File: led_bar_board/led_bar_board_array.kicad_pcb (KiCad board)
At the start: 2 copper layers, 90 x 98 mm, 720 parts, among them P1 Conn_01x01_Pin, P2 Conn_01x01_Pin, P3 Conn_01x01_Pin

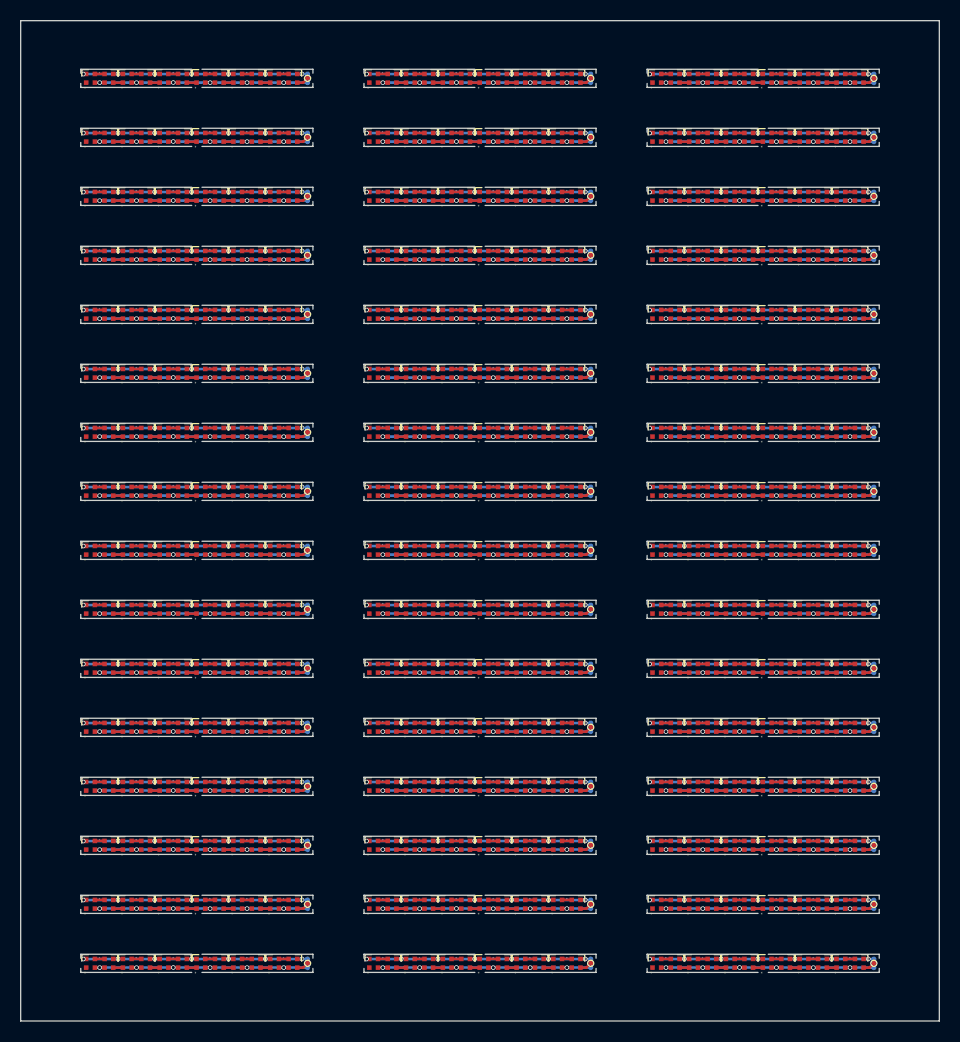
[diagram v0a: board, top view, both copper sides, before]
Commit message: feat(led_bar): modify shape and pad
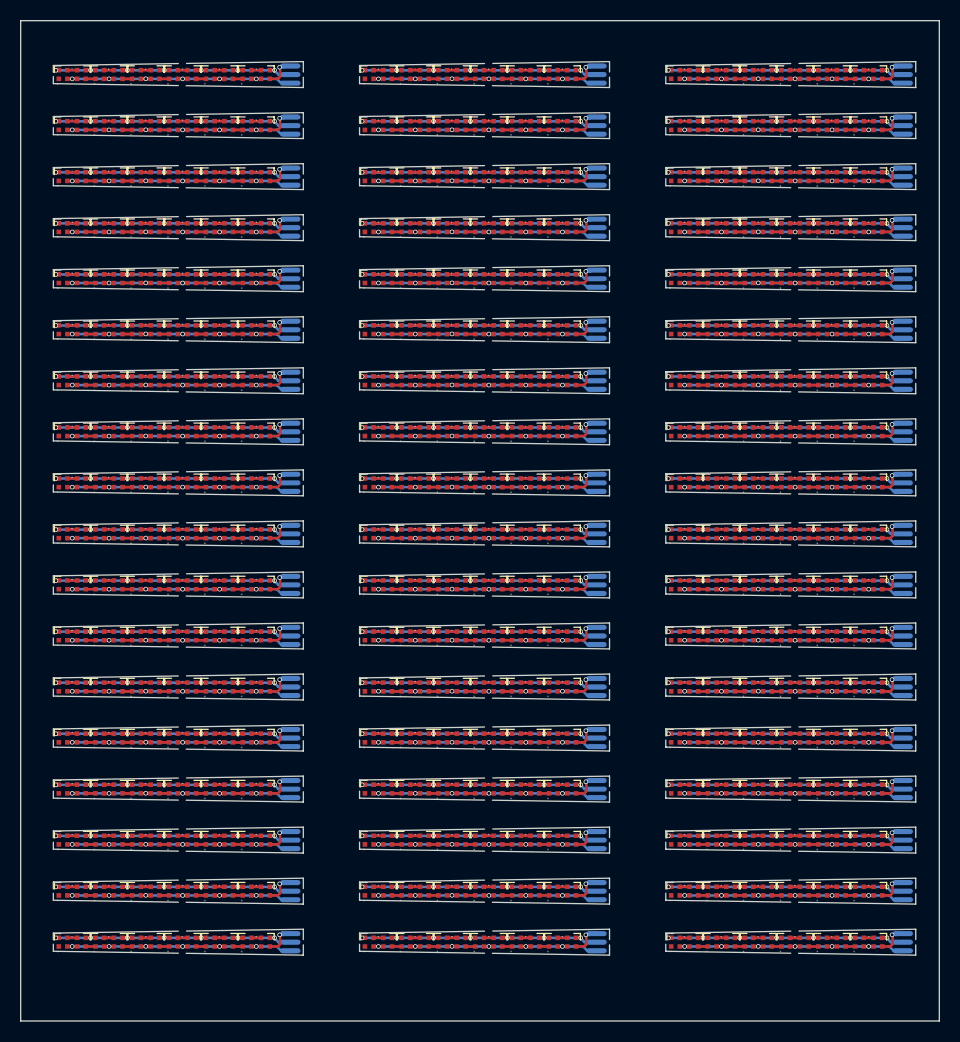
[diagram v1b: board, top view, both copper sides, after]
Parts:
- removed the D1 at (176.3, 62.4)
- removed the D1 at (120.8, 102.9)
- removed the D1 at (148.5, 62.4)
- removed the D1 at (120.8, 126.0)
- removed the D1 at (120.8, 50.9)
- removed the D1 at (120.8, 85.6)
- removed the D1 at (176.3, 137.6)
- removed the D1 at (148.5, 126.0)
- removed the D1 at (148.5, 108.7)
- removed the D1 at (176.3, 50.9)
- removed the D1 at (120.8, 108.7)
- removed the D1 at (148.5, 102.9)
- removed the D1 at (120.8, 68.2)
- removed the D1 at (176.3, 120.2)
- removed the D1 at (176.3, 79.8)
- removed the D1 at (148.5, 114.5)
- removed the D1 at (176.3, 114.5)
- removed the D1 at (120.8, 97.1)
- removed the D1 at (120.8, 74.0)
- removed the D1 at (148.5, 91.3)
- removed the D1 at (148.5, 56.7)
- removed the D1 at (148.5, 131.8)
- removed the D1 at (176.3, 102.9)
- removed the D1 at (148.5, 50.9)
- removed the D1 at (176.3, 97.1)
- removed the D1 at (148.5, 97.1)
- removed the D1 at (120.8, 62.4)
- removed the D1 at (148.5, 120.2)
- removed the D1 at (148.5, 74.0)
- removed the D1 at (120.8, 56.7)
- removed the D1 at (120.8, 131.8)
- removed the D1 at (120.8, 120.2)
- removed the D1 at (120.8, 114.5)
- removed the D1 at (176.3, 126.0)
- removed the D1 at (148.5, 68.2)
- removed the D1 at (176.3, 74.0)
- removed the D1 at (148.5, 85.6)
- removed the D1 at (176.3, 91.3)
- removed the D1 at (176.3, 85.6)
- removed the D1 at (148.5, 137.6)
- removed the D1 at (176.3, 68.2)
- removed the D1 at (176.3, 56.7)
- removed the D1 at (120.8, 137.6)
- removed the D1 at (176.3, 108.7)
- removed the D1 at (120.8, 79.8)
- removed the D1 at (176.3, 131.8)
- removed the D1 at (148.5, 79.8)
- removed the D1 at (120.8, 91.3)
- removed the D10 at (104.6, 108.7)
- removed the D10 at (132.3, 97.1)
- removed the D10 at (104.6, 79.8)
- removed the D10 at (160.0, 85.6)
- removed the D10 at (160.0, 97.1)
- removed the D10 at (104.6, 85.6)
- removed the D10 at (104.6, 56.7)
- removed the D10 at (160.0, 50.9)
- removed the D10 at (160.0, 126.0)
- removed the D10 at (132.3, 137.6)
- removed the D10 at (104.6, 114.5)
- removed the D10 at (160.0, 114.5)
- removed the D10 at (160.0, 74.0)
- removed the D10 at (132.3, 102.9)
- removed the D10 at (104.6, 91.3)
- removed the D10 at (132.3, 85.6)
- removed the D10 at (132.3, 108.7)
- removed the D10 at (132.3, 68.2)
- removed the D10 at (160.0, 102.9)
- removed the D10 at (104.6, 102.9)
- removed the D10 at (104.6, 137.6)
- removed the D10 at (132.3, 91.3)
- removed the D10 at (160.0, 131.8)
- removed the D10 at (160.0, 68.2)
- removed the D10 at (104.6, 97.1)
- removed the D10 at (104.6, 50.9)
- removed the D10 at (160.0, 62.4)
- removed the D10 at (104.6, 120.2)
- removed the D10 at (160.0, 56.7)
- removed the D10 at (132.3, 131.8)
- removed the D10 at (160.0, 91.3)
- removed the D10 at (132.3, 79.8)
- removed the D10 at (132.3, 56.7)
- removed the D10 at (104.6, 126.0)
- removed the D10 at (160.0, 108.7)
- removed the D10 at (132.3, 62.4)
- removed the D10 at (104.6, 74.0)
- removed the D10 at (104.6, 68.2)
- removed the D10 at (132.3, 120.2)
- removed the D10 at (132.3, 74.0)
- removed the D10 at (132.3, 114.5)
- removed the D10 at (104.6, 62.4)
- removed the D10 at (132.3, 50.9)
- removed the D10 at (160.0, 79.8)
- removed the D10 at (160.0, 137.6)
- removed the D10 at (160.0, 120.2)
- removed the D10 at (132.3, 126.0)
- removed the D10 at (104.6, 131.8)
- removed the D11 at (158.2, 108.7)
- removed the D11 at (102.8, 74.0)
- removed the D11 at (102.8, 114.5)
- removed the D11 at (102.8, 56.7)
- removed the D11 at (130.5, 120.2)
- removed the D11 at (130.5, 126.0)
- removed the D11 at (158.2, 91.3)
- removed the D11 at (158.2, 74.0)
- removed the D11 at (158.2, 50.9)
- removed the D11 at (158.2, 126.0)
- removed the D11 at (158.2, 79.8)
- removed the D11 at (130.5, 50.9)
- removed the D11 at (130.5, 68.2)
- removed the D11 at (102.8, 108.7)
- removed the D11 at (102.8, 126.0)
- removed the D11 at (158.2, 68.2)
- removed the D11 at (130.5, 91.3)
- removed the D11 at (102.8, 79.8)
- removed the D11 at (158.2, 131.8)
- removed the D11 at (102.8, 85.6)
- removed the D11 at (102.8, 50.9)
- removed the D11 at (130.5, 56.7)
- removed the D11 at (158.2, 85.6)
- removed the D11 at (102.8, 102.9)
- removed the D11 at (130.5, 137.6)
- removed the D11 at (158.2, 114.5)
- removed the D11 at (130.5, 85.6)
- removed the D11 at (102.8, 97.1)
- removed the D11 at (158.2, 56.7)
- removed the D11 at (130.5, 114.5)
- removed the D11 at (158.2, 62.4)
- removed the D11 at (130.5, 131.8)
- removed the D11 at (130.5, 108.7)
- removed the D11 at (158.2, 97.1)
- removed the D11 at (158.2, 137.6)
- removed the D11 at (130.5, 74.0)
- removed the D11 at (130.5, 102.9)
- removed the D11 at (102.8, 91.3)
- removed the D11 at (158.2, 120.2)
- removed the D11 at (102.8, 62.4)
- removed the D11 at (130.5, 79.8)
- removed the D11 at (102.8, 131.8)
- removed the D11 at (102.8, 137.6)
- removed the D11 at (130.5, 97.1)
- removed the D11 at (102.8, 68.2)
- removed the D11 at (102.8, 120.2)
- removed the D11 at (158.2, 102.9)
- removed the D11 at (130.5, 62.4)
- removed the D12 at (128.7, 79.8)
- removed the D12 at (101.0, 85.6)
- removed the D12 at (128.7, 120.2)
- removed the D12 at (156.4, 126.0)
- removed the D12 at (156.4, 85.6)
- removed the D12 at (156.4, 74.0)
- removed the D12 at (101.0, 62.4)
- removed the D12 at (128.7, 50.9)
- removed the D12 at (128.7, 68.2)
- removed the D12 at (101.0, 131.8)
- removed the D12 at (156.4, 91.3)
- removed the D12 at (128.7, 102.9)
- removed the D12 at (128.7, 126.0)
- removed the D12 at (156.4, 79.8)
- removed the D12 at (101.0, 102.9)
- removed the D12 at (128.7, 131.8)
- removed the D12 at (128.7, 108.7)
- removed the D12 at (156.4, 62.4)
- removed the D12 at (128.7, 85.6)
- removed the D12 at (101.0, 108.7)
- removed the D12 at (128.7, 74.0)
- removed the D12 at (156.4, 120.2)
- removed the D12 at (128.7, 91.3)
- removed the D12 at (101.0, 137.6)
- removed the D12 at (128.7, 114.5)
- removed the D12 at (101.0, 79.8)
- removed the D12 at (156.4, 102.9)
- removed the D12 at (101.0, 74.0)
- removed the D12 at (156.4, 131.8)
- removed the D12 at (156.4, 68.2)
- removed the D12 at (128.7, 56.7)
- removed the D12 at (101.0, 50.9)
- removed the D12 at (128.7, 62.4)
- removed the D12 at (101.0, 120.2)
- removed the D12 at (101.0, 68.2)
- removed the D12 at (101.0, 114.5)
- removed the D12 at (156.4, 137.6)
- removed the D12 at (156.4, 50.9)
- removed the D12 at (128.7, 97.1)
- removed the D12 at (101.0, 91.3)
- removed the D12 at (128.7, 137.6)
- removed the D12 at (101.0, 56.7)
- removed the D12 at (156.4, 56.7)
- removed the D12 at (101.0, 97.1)
- removed the D12 at (156.4, 108.7)
- removed the D12 at (156.4, 114.5)
- removed the D12 at (101.0, 126.0)
- removed the D12 at (156.4, 97.1)
- removed the D2 at (119.0, 68.2)
- removed the D2 at (146.7, 50.9)
- removed the D2 at (119.0, 74.0)
- removed the D2 at (119.0, 126.0)
- removed the D2 at (119.0, 50.9)
- removed the D2 at (146.7, 79.8)
- removed the D2 at (146.7, 120.2)
- removed the D2 at (119.0, 62.4)
- removed the D2 at (146.7, 62.4)
- removed the D2 at (146.7, 68.2)
- removed the D2 at (146.7, 74.0)
- removed the D2 at (119.0, 85.6)
- removed the D2 at (119.0, 131.8)
- removed the D2 at (174.5, 91.3)
- removed the D2 at (146.7, 126.0)
- removed the D2 at (146.7, 97.1)
- removed the D2 at (119.0, 91.3)
- removed the D2 at (119.0, 137.6)
- removed the D2 at (174.5, 74.0)
- removed the D2 at (174.5, 85.6)
- removed the D2 at (174.5, 137.6)
- removed the D2 at (174.5, 62.4)
- removed the D2 at (174.5, 50.9)
- removed the D2 at (119.0, 114.5)
- removed the D2 at (146.7, 131.8)
- removed the D2 at (119.0, 108.7)
- removed the D2 at (174.5, 68.2)
- removed the D2 at (174.5, 114.5)
- removed the D2 at (174.5, 97.1)
- removed the D2 at (146.7, 114.5)
- removed the D2 at (146.7, 56.7)
- removed the D2 at (174.5, 120.2)
- removed the D2 at (119.0, 79.8)
- removed the D2 at (174.5, 131.8)
- removed the D2 at (174.5, 108.7)
- removed the D2 at (146.7, 91.3)
- removed the D2 at (119.0, 120.2)
- removed the D2 at (174.5, 56.7)
- removed the D2 at (146.7, 102.9)
- removed the D2 at (174.5, 102.9)
- removed the D2 at (146.7, 108.7)
- removed the D2 at (174.5, 126.0)
- removed the D2 at (119.0, 97.1)
- removed the D2 at (119.0, 102.9)
- removed the D2 at (119.0, 56.7)
- removed the D2 at (174.5, 79.8)
- removed the D2 at (146.7, 85.6)
- removed the D2 at (146.7, 137.6)
- removed the D3 at (117.2, 114.5)
- removed the D3 at (144.9, 102.9)
- removed the D3 at (144.9, 68.2)
- removed the D3 at (144.9, 131.8)
- removed the D3 at (144.9, 79.8)
- removed the D3 at (144.9, 120.2)
- removed the D3 at (172.7, 62.4)
- removed the D3 at (117.2, 79.8)
- removed the D3 at (144.9, 56.7)
- removed the D3 at (144.9, 85.6)
- removed the D3 at (117.2, 108.7)
- removed the D3 at (172.7, 85.6)
- removed the D3 at (172.7, 131.8)
- removed the D3 at (144.9, 137.6)
- removed the D3 at (172.7, 50.9)
- removed the D3 at (117.2, 62.4)
- removed the D3 at (144.9, 97.1)
- removed the D3 at (172.7, 74.0)
- removed the D3 at (117.2, 74.0)
- removed the D3 at (117.2, 102.9)
- removed the D3 at (172.7, 108.7)
- removed the D3 at (117.2, 97.1)
- removed the D3 at (144.9, 108.7)
- removed the D3 at (144.9, 74.0)
- removed the D3 at (172.7, 68.2)
- removed the D3 at (144.9, 91.3)
- removed the D3 at (172.7, 126.0)
- removed the D3 at (144.9, 114.5)
- removed the D3 at (117.2, 68.2)
- removed the D3 at (117.2, 126.0)
- removed the D3 at (172.7, 102.9)
- removed the D3 at (172.7, 97.1)
- removed the D3 at (117.2, 131.8)
- removed the D3 at (117.2, 137.6)
- removed the D3 at (172.7, 137.6)
- removed the D3 at (172.7, 56.7)
- removed the D3 at (117.2, 91.3)
- removed the D3 at (172.7, 120.2)
- removed the D3 at (144.9, 62.4)
- removed the D3 at (172.7, 114.5)
- removed the D3 at (117.2, 85.6)
- removed the D3 at (117.2, 56.7)
- removed the D3 at (172.7, 79.8)
- removed the D3 at (144.9, 126.0)
- removed the D3 at (117.2, 50.9)
- removed the D3 at (172.7, 91.3)
- removed the D3 at (117.2, 120.2)
- removed the D3 at (144.9, 50.9)
- removed the D4 at (115.4, 62.4)
- removed the D4 at (143.1, 137.6)
- removed the D4 at (143.1, 131.8)
- removed the D4 at (170.9, 102.9)
- removed the D4 at (115.4, 126.0)
- removed the D4 at (143.1, 50.9)
- removed the D4 at (115.4, 97.1)
- removed the D4 at (115.4, 91.3)
- removed the D4 at (115.4, 85.6)
- removed the D4 at (143.1, 56.7)
- removed the D4 at (115.4, 50.9)
- removed the D4 at (170.9, 131.8)
- removed the D4 at (170.9, 120.2)
- removed the D4 at (143.1, 120.2)
- removed the D4 at (170.9, 137.6)
- removed the D4 at (115.4, 114.5)
- removed the D4 at (143.1, 68.2)
- removed the D4 at (170.9, 85.6)
- removed the D4 at (170.9, 74.0)
- removed the D4 at (143.1, 85.6)
- removed the D4 at (170.9, 126.0)
- removed the D4 at (115.4, 108.7)
- removed the D4 at (143.1, 108.7)
- removed the D4 at (115.4, 131.8)
- removed the D4 at (143.1, 102.9)
- removed the D4 at (143.1, 97.1)
- removed the D4 at (170.9, 68.2)
- removed the D4 at (143.1, 74.0)
- removed the D4 at (170.9, 62.4)
- removed the D4 at (115.4, 74.0)
- removed the D4 at (170.9, 56.7)
- removed the D4 at (115.4, 120.2)
- removed the D4 at (170.9, 91.3)
- removed the D4 at (170.9, 114.5)
- removed the D4 at (170.9, 50.9)
- removed the D4 at (143.1, 62.4)
- removed the D4 at (115.4, 102.9)
- removed the D4 at (115.4, 56.7)
- removed the D4 at (143.1, 126.0)
- removed the D4 at (143.1, 114.5)
- removed the D4 at (143.1, 79.8)
- removed the D4 at (115.4, 79.8)
- removed the D4 at (170.9, 108.7)
- removed the D4 at (170.9, 79.8)
- removed the D4 at (115.4, 137.6)
- removed the D4 at (143.1, 91.3)
- removed the D4 at (170.9, 97.1)
- removed the D4 at (115.4, 68.2)
- removed the D5 at (169.1, 126.0)
- removed the D5 at (113.6, 102.9)
- removed the D5 at (113.6, 108.7)
- removed the D5 at (113.6, 126.0)
- removed the D5 at (113.6, 97.1)
- removed the D5 at (169.1, 62.4)
- removed the D5 at (113.6, 56.7)
- removed the D5 at (141.3, 50.9)
- removed the D5 at (141.3, 102.9)
- removed the D5 at (113.6, 91.3)
- removed the D5 at (141.3, 114.5)
- removed the D5 at (113.6, 137.6)
- removed the D5 at (169.1, 120.2)
- removed the D5 at (169.1, 74.0)
- removed the D5 at (141.3, 97.1)
- removed the D5 at (169.1, 108.7)
- removed the D5 at (169.1, 114.5)
- removed the D5 at (113.6, 68.2)
- removed the D5 at (141.3, 85.6)
- removed the D5 at (169.1, 102.9)
- removed the D5 at (113.6, 74.0)
- removed the D5 at (141.3, 74.0)
- removed the D5 at (141.3, 137.6)
- removed the D5 at (169.1, 50.9)
- removed the D5 at (141.3, 68.2)
- removed the D5 at (141.3, 56.7)
- removed the D5 at (141.3, 79.8)
- removed the D5 at (113.6, 50.9)
- removed the D5 at (169.1, 79.8)
- removed the D5 at (113.6, 85.6)
- removed the D5 at (141.3, 62.4)
- removed the D5 at (141.3, 120.2)
- removed the D5 at (113.6, 131.8)
- removed the D5 at (113.6, 79.8)
- removed the D5 at (169.1, 137.6)
- removed the D5 at (169.1, 56.7)
- removed the D5 at (113.6, 114.5)
- removed the D5 at (169.1, 85.6)
- removed the D5 at (113.6, 120.2)
- removed the D5 at (169.1, 91.3)
- removed the D5 at (141.3, 91.3)
- removed the D5 at (169.1, 68.2)
- removed the D5 at (113.6, 62.4)
- removed the D5 at (169.1, 97.1)
- removed the D5 at (141.3, 126.0)
- removed the D5 at (141.3, 108.7)
- removed the D5 at (141.3, 131.8)
- removed the D5 at (169.1, 131.8)
- removed the D6 at (139.5, 120.2)
- removed the D6 at (167.2, 62.4)
- removed the D6 at (111.8, 68.2)
- removed the D6 at (139.5, 68.2)
- removed the D6 at (139.5, 79.8)
- removed the D6 at (167.2, 126.0)
- removed the D6 at (139.5, 91.3)
- removed the D6 at (111.8, 74.0)
- removed the D6 at (167.2, 74.0)
- removed the D6 at (139.5, 97.1)
- removed the D6 at (111.8, 126.0)
- removed the D6 at (167.2, 137.6)
- removed the D6 at (167.2, 56.7)
- removed the D6 at (111.8, 102.9)
- removed the D6 at (167.2, 68.2)
- removed the D6 at (111.8, 137.6)
- removed the D6 at (111.8, 62.4)
- removed the D6 at (111.8, 79.8)
- removed the D6 at (139.5, 62.4)
- removed the D6 at (167.2, 120.2)
- removed the D6 at (167.2, 91.3)
- removed the D6 at (111.8, 56.7)
- removed the D6 at (139.5, 102.9)
- removed the D6 at (139.5, 74.0)
- removed the D6 at (111.8, 50.9)
- removed the D6 at (167.2, 85.6)
- removed the D6 at (167.2, 97.1)
- removed the D6 at (111.8, 131.8)
- removed the D6 at (139.5, 85.6)
- removed the D6 at (167.2, 108.7)
- removed the D6 at (167.2, 131.8)
- removed the D6 at (111.8, 108.7)
- removed the D6 at (111.8, 97.1)
- removed the D6 at (139.5, 131.8)
- removed the D6 at (111.8, 114.5)
- removed the D6 at (167.2, 102.9)
- removed the D6 at (139.5, 114.5)
- removed the D6 at (167.2, 79.8)
- removed the D6 at (139.5, 108.7)
- removed the D6 at (139.5, 50.9)
- removed the D6 at (139.5, 137.6)
- removed the D6 at (111.8, 85.6)
- removed the D6 at (111.8, 120.2)
- removed the D6 at (139.5, 126.0)
- removed the D6 at (167.2, 50.9)
- removed the D6 at (139.5, 56.7)
- removed the D6 at (167.2, 114.5)
- removed the D6 at (111.8, 91.3)
- removed the D7 at (137.7, 79.8)
- removed the D7 at (165.4, 91.3)
- removed the D7 at (165.4, 74.0)
- removed the D7 at (165.4, 85.6)
- removed the D7 at (165.4, 50.9)
- removed the D7 at (110.0, 126.0)
- removed the D7 at (110.0, 68.2)
- removed the D7 at (137.7, 91.3)
- removed the D7 at (110.0, 79.8)
- removed the D7 at (110.0, 85.6)
- removed the D7 at (165.4, 56.7)
- removed the D7 at (110.0, 114.5)
- removed the D7 at (137.7, 85.6)
- removed the D7 at (110.0, 137.6)
- removed the D7 at (165.4, 137.6)
- removed the D7 at (110.0, 74.0)
- removed the D7 at (110.0, 97.1)
- removed the D7 at (110.0, 50.9)
- removed the D7 at (137.7, 97.1)
- removed the D7 at (110.0, 91.3)
- removed the D7 at (165.4, 62.4)
- removed the D7 at (110.0, 102.9)
- removed the D7 at (110.0, 56.7)
- removed the D7 at (137.7, 108.7)
- removed the D7 at (165.4, 131.8)
- removed the D7 at (137.7, 137.6)
- removed the D7 at (137.7, 56.7)
- removed the D7 at (137.7, 68.2)
- removed the D7 at (165.4, 114.5)
- removed the D7 at (137.7, 120.2)
- removed the D7 at (165.4, 68.2)
- removed the D7 at (110.0, 62.4)
- removed the D7 at (165.4, 120.2)
- removed the D7 at (110.0, 131.8)
- removed the D7 at (165.4, 102.9)
- removed the D7 at (165.4, 79.8)
- removed the D7 at (137.7, 114.5)
- removed the D7 at (137.7, 102.9)
- removed the D7 at (137.7, 74.0)
- removed the D7 at (137.7, 50.9)
- removed the D7 at (110.0, 120.2)
- removed the D7 at (165.4, 108.7)
- removed the D7 at (110.0, 108.7)
- removed the D7 at (137.7, 126.0)
- removed the D7 at (137.7, 62.4)
- removed the D7 at (165.4, 126.0)
- removed the D7 at (165.4, 97.1)
- removed the D7 at (137.7, 131.8)
- removed the D8 at (108.2, 114.5)
- removed the D8 at (163.6, 120.2)
- removed the D8 at (108.2, 68.2)
- removed the D8 at (108.2, 97.1)
- removed the D8 at (135.9, 79.8)
- removed the D8 at (108.2, 120.2)
- removed the D8 at (163.6, 74.0)
- removed the D8 at (163.6, 68.2)
- removed the D8 at (108.2, 137.6)
- removed the D8 at (135.9, 62.4)
- removed the D8 at (135.9, 120.2)
- removed the D8 at (135.9, 85.6)
- removed the D8 at (163.6, 79.8)
- removed the D8 at (108.2, 74.0)
- removed the D8 at (108.2, 62.4)
- removed the D8 at (163.6, 91.3)
- removed the D8 at (163.6, 114.5)
- removed the D8 at (135.9, 50.9)
- removed the D8 at (135.9, 131.8)
- removed the D8 at (135.9, 108.7)
- removed the D8 at (135.9, 74.0)
- removed the D8 at (108.2, 50.9)
- removed the D8 at (108.2, 108.7)
- removed the D8 at (163.6, 85.6)
- removed the D8 at (163.6, 97.1)
- removed the D8 at (135.9, 97.1)
- removed the D8 at (135.9, 126.0)
- removed the D8 at (135.9, 68.2)
- removed the D8 at (163.6, 131.8)
- removed the D8 at (163.6, 126.0)
- removed the D8 at (108.2, 56.7)
- removed the D8 at (108.2, 85.6)
- removed the D8 at (135.9, 56.7)
- removed the D8 at (108.2, 102.9)
- removed the D8 at (108.2, 79.8)
- removed the D8 at (163.6, 102.9)
- removed the D8 at (108.2, 131.8)
- removed the D8 at (163.6, 56.7)
- removed the D8 at (135.9, 114.5)
- removed the D8 at (108.2, 126.0)
- removed the D8 at (135.9, 102.9)
- removed the D8 at (163.6, 62.4)
- removed the D8 at (135.9, 91.3)
- removed the D8 at (163.6, 137.6)
- removed the D8 at (135.9, 137.6)
- removed the D8 at (163.6, 50.9)
- removed the D8 at (108.2, 91.3)
- removed the D8 at (163.6, 108.7)
- removed the D9 at (161.8, 108.7)
- removed the D9 at (134.1, 102.9)
- removed the D9 at (106.4, 91.3)
- removed the D9 at (134.1, 120.2)
- removed the D9 at (106.4, 126.0)
- removed the D9 at (106.4, 137.6)
- removed the D9 at (161.8, 74.0)
- removed the D9 at (161.8, 120.2)
- removed the D9 at (161.8, 79.8)
- removed the D9 at (106.4, 68.2)
- removed the D9 at (106.4, 74.0)
- removed the D9 at (134.1, 68.2)
- removed the D9 at (106.4, 131.8)
- removed the D9 at (106.4, 62.4)
- removed the D9 at (161.8, 62.4)
- removed the D9 at (161.8, 126.0)
- removed the D9 at (161.8, 114.5)
- removed the D9 at (106.4, 85.6)
- removed the D9 at (134.1, 79.8)
- removed the D9 at (134.1, 85.6)
- removed the D9 at (106.4, 97.1)
- removed the D9 at (161.8, 97.1)
- removed the D9 at (161.8, 56.7)
- removed the D9 at (134.1, 131.8)
- removed the D9 at (134.1, 56.7)
- removed the D9 at (106.4, 102.9)
- removed the D9 at (106.4, 114.5)
- removed the D9 at (134.1, 108.7)
- removed the D9 at (134.1, 91.3)
- removed the D9 at (134.1, 62.4)
- removed the D9 at (134.1, 137.6)
- removed the D9 at (106.4, 79.8)
- removed the D9 at (161.8, 102.9)
- removed the D9 at (134.1, 114.5)
- removed the D9 at (134.1, 50.9)
- removed the D9 at (161.8, 91.3)
- removed the D9 at (134.1, 126.0)
- removed the D9 at (134.1, 97.1)
- removed the D9 at (134.1, 74.0)
- removed the D9 at (161.8, 50.9)
- removed the D9 at (161.8, 85.6)
- removed the D9 at (106.4, 108.7)
- removed the D9 at (161.8, 137.6)
- removed the D9 at (106.4, 56.7)
- removed the D9 at (161.8, 131.8)
- removed the D9 at (161.8, 68.2)
- removed the D9 at (106.4, 50.9)
- removed the D9 at (106.4, 120.2)
- removed the P1 at (177.7, 79.4)
- removed the P1 at (150.0, 102.5)
- removed the P1 at (177.7, 131.4)
- removed the P1 at (122.2, 67.8)
- removed the P1 at (122.2, 125.6)
- removed the P1 at (150.0, 85.2)
- removed the P1 at (150.0, 125.6)
- removed the P1 at (177.7, 56.2)
- removed the P1 at (177.7, 96.7)
- removed the P1 at (122.2, 114.0)
- removed the P1 at (122.2, 85.2)
- removed the P1 at (177.7, 119.8)
- removed the P1 at (177.7, 102.5)
- removed the P1 at (177.7, 85.2)
- removed the P1 at (177.7, 62.0)
- removed the P1 at (122.2, 90.9)
- removed the P1 at (150.0, 56.2)
- removed the P1 at (122.2, 119.8)
- removed the P1 at (122.2, 137.2)
- removed the P1 at (122.2, 62.0)
- removed the P1 at (122.2, 56.2)
- removed the P1 at (122.2, 50.5)
- removed the P1 at (150.0, 114.0)
- removed the P1 at (150.0, 50.5)
- removed the P1 at (150.0, 119.8)
- removed the P1 at (150.0, 108.3)
- removed the P1 at (150.0, 73.6)
- removed the P1 at (177.7, 73.6)
- removed the P1 at (150.0, 79.4)
- removed the P1 at (177.7, 125.6)
- removed the P1 at (177.7, 114.0)
- removed the P1 at (122.2, 73.6)
- removed the P1 at (122.2, 79.4)
- removed the P1 at (150.0, 131.4)
- removed the P1 at (177.7, 108.3)
- removed the P1 at (150.0, 67.8)
- removed the P1 at (122.2, 131.4)
- removed the P1 at (177.7, 90.9)
- removed the P1 at (177.7, 67.8)
- removed the P1 at (177.7, 137.2)
- removed the P1 at (150.0, 62.0)
- removed the P1 at (122.2, 102.5)
- removed the P1 at (177.7, 50.5)
- removed the P1 at (150.0, 137.2)
- removed the P1 at (122.2, 96.7)
- removed the P1 at (150.0, 96.7)
- removed the P1 at (150.0, 90.9)
- removed the P1 at (122.2, 108.3)
- removed the P2 at (122.2, 56.7)
- removed the P2 at (122.2, 74.0)
- removed the P2 at (150.0, 108.7)
- removed the P2 at (122.2, 137.6)
- removed the P2 at (177.7, 68.2)
- removed the P2 at (122.2, 131.8)
- removed the P2 at (150.0, 131.8)
- removed the P2 at (177.7, 97.1)
- removed the P2 at (177.7, 126.0)
- removed the P2 at (177.7, 131.8)
- removed the P2 at (150.0, 120.2)
- removed the P2 at (177.7, 74.0)
- removed the P2 at (150.0, 102.9)
- removed the P2 at (150.0, 114.5)
- removed the P2 at (150.0, 74.0)
- removed the P2 at (177.7, 120.2)
- removed the P2 at (122.2, 50.9)
- removed the P2 at (177.7, 79.8)
- removed the P2 at (150.0, 85.6)
- removed the P2 at (150.0, 97.1)
- removed the P2 at (122.2, 97.1)
- removed the P2 at (122.2, 102.9)
- removed the P2 at (122.2, 108.7)
- removed the P2 at (122.2, 85.6)
- removed the P2 at (122.2, 114.5)
- removed the P2 at (177.7, 50.9)
- removed the P2 at (177.7, 62.5)
- removed the P2 at (122.2, 120.2)
- removed the P2 at (150.0, 126.0)
- removed the P2 at (177.7, 114.5)
- removed the P2 at (122.2, 79.8)
- removed the P2 at (177.7, 56.7)
- removed the P2 at (150.0, 56.7)
- removed the P2 at (177.7, 108.7)
- removed the P2 at (177.7, 91.3)
- removed the P2 at (150.0, 68.2)
- removed the P2 at (177.7, 85.6)
- removed the P2 at (122.2, 68.2)
- removed the P2 at (177.7, 102.9)
- removed the P2 at (122.2, 91.3)
- removed the P2 at (150.0, 91.3)
- removed the P2 at (150.0, 79.8)
- removed the P2 at (150.0, 62.5)
- removed the P2 at (150.0, 50.9)
- removed the P2 at (122.2, 62.5)
- removed the P2 at (150.0, 137.6)
- removed the P2 at (177.7, 137.6)
- removed the P2 at (122.2, 126.0)
- removed the P3 at (122.2, 86.0)
- removed the P3 at (177.7, 80.2)
- removed the P3 at (177.7, 138.0)
- removed the P3 at (150.0, 97.5)
- removed the P3 at (150.0, 51.3)
- removed the P3 at (150.0, 62.9)
- removed the P3 at (122.2, 114.9)
- removed the P3 at (177.7, 68.7)
- removed the P3 at (150.0, 138.0)
- removed the P3 at (150.0, 68.7)
- removed the P3 at (177.7, 86.0)
- removed the P3 at (150.0, 126.5)
- removed the P3 at (122.2, 103.3)
- removed the P3 at (177.7, 51.3)
- removed the P3 at (122.2, 126.5)
- removed the P3 at (122.2, 57.1)
- removed the P3 at (122.2, 80.2)
- removed the P3 at (122.2, 120.7)
- removed the P3 at (122.2, 68.7)
- removed the P3 at (150.0, 109.1)
- removed the P3 at (122.2, 51.3)
- removed the P3 at (177.7, 57.1)
- removed the P3 at (122.2, 62.9)
- removed the P3 at (177.7, 62.9)
- removed the P3 at (177.7, 74.4)
- removed the P3 at (150.0, 103.3)
- removed the P3 at (177.7, 120.7)
- removed the P3 at (150.0, 86.0)
- removed the P3 at (122.2, 138.0)
- removed the P3 at (122.2, 109.1)
- removed the P3 at (122.2, 74.4)
- removed the P3 at (150.0, 74.4)
- removed the P3 at (177.7, 109.1)
- removed the P3 at (150.0, 132.2)
- removed the P3 at (177.7, 103.3)
- removed the P3 at (177.7, 97.5)
- removed the P3 at (177.7, 126.5)
- removed the P3 at (150.0, 91.8)
- removed the P3 at (150.0, 120.7)
- removed the P3 at (177.7, 132.2)
- removed the P3 at (150.0, 80.2)
- removed the P3 at (122.2, 91.8)
- removed the P3 at (150.0, 114.9)
- removed the P3 at (150.0, 57.1)
- removed the P3 at (177.7, 91.8)
- removed the P3 at (122.2, 97.5)
- removed the P3 at (177.7, 114.9)
- removed the P3 at (122.2, 132.2)
- added D1: WS6812, LED_SMD:LED_SK6812_EC15_1.5x1.5mm, F.Cu at (118.1, 95.5)
- added D1: WS6812, LED_SMD:LED_SK6812_EC15_1.5x1.5mm, F.Cu at (178.1, 90.5)
- added D1: WS6812, LED_SMD:LED_SK6812_EC15_1.5x1.5mm, F.Cu at (178.1, 105.5)
- added D1: WS6812, LED_SMD:LED_SK6812_EC15_1.5x1.5mm, F.Cu at (118.1, 110.5)
- added D1: WS6812, LED_SMD:LED_SK6812_EC15_1.5x1.5mm, F.Cu at (118.1, 80.5)
- added D1: WS6812, LED_SMD:LED_SK6812_EC15_1.5x1.5mm, F.Cu at (178.1, 95.5)
- added D1: WS6812, LED_SMD:LED_SK6812_EC15_1.5x1.5mm, F.Cu at (178.1, 125.5)
- added D1: WS6812, LED_SMD:LED_SK6812_EC15_1.5x1.5mm, F.Cu at (148.1, 75.5)
- added D1: WS6812, LED_SMD:LED_SK6812_EC15_1.5x1.5mm, F.Cu at (118.1, 115.5)
- added D1: WS6812, LED_SMD:LED_SK6812_EC15_1.5x1.5mm, F.Cu at (178.1, 75.5)
- added D1: WS6812, LED_SMD:LED_SK6812_EC15_1.5x1.5mm, F.Cu at (148.1, 95.5)
- added D1: WS6812, LED_SMD:LED_SK6812_EC15_1.5x1.5mm, F.Cu at (148.1, 85.5)
- added D1: WS6812, LED_SMD:LED_SK6812_EC15_1.5x1.5mm, F.Cu at (118.1, 135.5)
- added D1: WS6812, LED_SMD:LED_SK6812_EC15_1.5x1.5mm, F.Cu at (148.1, 90.5)
- added D1: WS6812, LED_SMD:LED_SK6812_EC15_1.5x1.5mm, F.Cu at (178.1, 135.5)
- added D1: WS6812, LED_SMD:LED_SK6812_EC15_1.5x1.5mm, F.Cu at (178.1, 85.5)
- added D1: WS6812, LED_SMD:LED_SK6812_EC15_1.5x1.5mm, F.Cu at (118.1, 70.5)
- added D1: WS6812, LED_SMD:LED_SK6812_EC15_1.5x1.5mm, F.Cu at (118.1, 75.5)
- added D1: WS6812, LED_SMD:LED_SK6812_EC15_1.5x1.5mm, F.Cu at (178.1, 50.5)
- added D1: WS6812, LED_SMD:LED_SK6812_EC15_1.5x1.5mm, F.Cu at (118.1, 50.5)
- added D1: WS6812, LED_SMD:LED_SK6812_EC15_1.5x1.5mm, F.Cu at (148.1, 60.5)
- added D1: WS6812, LED_SMD:LED_SK6812_EC15_1.5x1.5mm, F.Cu at (148.1, 80.5)
- added D1: WS6812, LED_SMD:LED_SK6812_EC15_1.5x1.5mm, F.Cu at (148.1, 55.5)
- added D1: WS6812, LED_SMD:LED_SK6812_EC15_1.5x1.5mm, F.Cu at (178.1, 100.5)
- added D1: WS6812, LED_SMD:LED_SK6812_EC15_1.5x1.5mm, F.Cu at (178.1, 60.5)
- added D1: WS6812, LED_SMD:LED_SK6812_EC15_1.5x1.5mm, F.Cu at (148.1, 105.5)
- added D1: WS6812, LED_SMD:LED_SK6812_EC15_1.5x1.5mm, F.Cu at (178.1, 130.5)
- added D1: WS6812, LED_SMD:LED_SK6812_EC15_1.5x1.5mm, F.Cu at (118.1, 85.5)
- added D1: WS6812, LED_SMD:LED_SK6812_EC15_1.5x1.5mm, F.Cu at (148.1, 110.5)
- added D1: WS6812, LED_SMD:LED_SK6812_EC15_1.5x1.5mm, F.Cu at (148.1, 135.5)
- added D1: WS6812, LED_SMD:LED_SK6812_EC15_1.5x1.5mm, F.Cu at (118.1, 90.5)
- added D1: WS6812, LED_SMD:LED_SK6812_EC15_1.5x1.5mm, F.Cu at (118.1, 120.5)
- added D1: WS6812, LED_SMD:LED_SK6812_EC15_1.5x1.5mm, F.Cu at (178.1, 70.5)
- added D1: WS6812, LED_SMD:LED_SK6812_EC15_1.5x1.5mm, F.Cu at (118.1, 60.5)
- added D1: WS6812, LED_SMD:LED_SK6812_EC15_1.5x1.5mm, F.Cu at (178.1, 120.5)
- added D1: WS6812, LED_SMD:LED_SK6812_EC15_1.5x1.5mm, F.Cu at (118.1, 100.5)
- added D1: WS6812, LED_SMD:LED_SK6812_EC15_1.5x1.5mm, F.Cu at (148.1, 115.5)
- added D1: WS6812, LED_SMD:LED_SK6812_EC15_1.5x1.5mm, F.Cu at (148.1, 50.5)
- added D1: WS6812, LED_SMD:LED_SK6812_EC15_1.5x1.5mm, F.Cu at (178.1, 110.5)
- added D1: WS6812, LED_SMD:LED_SK6812_EC15_1.5x1.5mm, F.Cu at (148.1, 120.5)
- added D1: WS6812, LED_SMD:LED_SK6812_EC15_1.5x1.5mm, F.Cu at (118.1, 130.5)
- added D1: WS6812, LED_SMD:LED_SK6812_EC15_1.5x1.5mm, F.Cu at (178.1, 65.5)
- added D1: WS6812, LED_SMD:LED_SK6812_EC15_1.5x1.5mm, F.Cu at (148.1, 100.5)
- added D1: WS6812, LED_SMD:LED_SK6812_EC15_1.5x1.5mm, F.Cu at (178.1, 80.5)
- added D1: WS6812, LED_SMD:LED_SK6812_EC15_1.5x1.5mm, F.Cu at (148.1, 65.5)
- added D1: WS6812, LED_SMD:LED_SK6812_EC15_1.5x1.5mm, F.Cu at (118.1, 105.5)
- added D1: WS6812, LED_SMD:LED_SK6812_EC15_1.5x1.5mm, F.Cu at (148.1, 125.5)
- added D1: WS6812, LED_SMD:LED_SK6812_EC15_1.5x1.5mm, F.Cu at (118.1, 125.5)
- added D1: WS6812, LED_SMD:LED_SK6812_EC15_1.5x1.5mm, F.Cu at (178.1, 55.5)
- added D1: WS6812, LED_SMD:LED_SK6812_EC15_1.5x1.5mm, F.Cu at (178.1, 115.5)
- added D1: WS6812, LED_SMD:LED_SK6812_EC15_1.5x1.5mm, F.Cu at (148.1, 130.5)
- added D1: WS6812, LED_SMD:LED_SK6812_EC15_1.5x1.5mm, F.Cu at (118.1, 65.5)
- added D1: WS6812, LED_SMD:LED_SK6812_EC15_1.5x1.5mm, F.Cu at (148.1, 70.5)
- added D1: WS6812, LED_SMD:LED_SK6812_EC15_1.5x1.5mm, F.Cu at (118.1, 55.5)
- added D10: WS6812, LED_SMD:LED_SK6812_EC15_1.5x1.5mm, F.Cu at (161.9, 75.5)
- added D10: WS6812, LED_SMD:LED_SK6812_EC15_1.5x1.5mm, F.Cu at (101.9, 50.5)
- added D10: WS6812, LED_SMD:LED_SK6812_EC15_1.5x1.5mm, F.Cu at (131.9, 115.5)
- added D10: WS6812, LED_SMD:LED_SK6812_EC15_1.5x1.5mm, F.Cu at (131.9, 105.5)
- added D10: WS6812, LED_SMD:LED_SK6812_EC15_1.5x1.5mm, F.Cu at (161.9, 65.5)
- added D10: WS6812, LED_SMD:LED_SK6812_EC15_1.5x1.5mm, F.Cu at (101.9, 100.5)
- added D10: WS6812, LED_SMD:LED_SK6812_EC15_1.5x1.5mm, F.Cu at (161.9, 95.5)
- added D10: WS6812, LED_SMD:LED_SK6812_EC15_1.5x1.5mm, F.Cu at (161.9, 135.5)
- added D10: WS6812, LED_SMD:LED_SK6812_EC15_1.5x1.5mm, F.Cu at (161.9, 120.5)
- added D10: WS6812, LED_SMD:LED_SK6812_EC15_1.5x1.5mm, F.Cu at (101.9, 110.5)
- added D10: WS6812, LED_SMD:LED_SK6812_EC15_1.5x1.5mm, F.Cu at (161.9, 130.5)
- added D10: WS6812, LED_SMD:LED_SK6812_EC15_1.5x1.5mm, F.Cu at (131.9, 60.5)
- added D10: WS6812, LED_SMD:LED_SK6812_EC15_1.5x1.5mm, F.Cu at (131.9, 100.5)
- added D10: WS6812, LED_SMD:LED_SK6812_EC15_1.5x1.5mm, F.Cu at (161.9, 90.5)
- added D10: WS6812, LED_SMD:LED_SK6812_EC15_1.5x1.5mm, F.Cu at (131.9, 130.5)
- added D10: WS6812, LED_SMD:LED_SK6812_EC15_1.5x1.5mm, F.Cu at (161.9, 85.5)
- added D10: WS6812, LED_SMD:LED_SK6812_EC15_1.5x1.5mm, F.Cu at (131.9, 90.5)
- added D10: WS6812, LED_SMD:LED_SK6812_EC15_1.5x1.5mm, F.Cu at (161.9, 110.5)
- added D10: WS6812, LED_SMD:LED_SK6812_EC15_1.5x1.5mm, F.Cu at (101.9, 90.5)
- added D10: WS6812, LED_SMD:LED_SK6812_EC15_1.5x1.5mm, F.Cu at (161.9, 80.5)
- added D10: WS6812, LED_SMD:LED_SK6812_EC15_1.5x1.5mm, F.Cu at (161.9, 100.5)
- added D10: WS6812, LED_SMD:LED_SK6812_EC15_1.5x1.5mm, F.Cu at (101.9, 70.5)
- added D10: WS6812, LED_SMD:LED_SK6812_EC15_1.5x1.5mm, F.Cu at (131.9, 80.5)
- added D10: WS6812, LED_SMD:LED_SK6812_EC15_1.5x1.5mm, F.Cu at (161.9, 55.5)
- added D10: WS6812, LED_SMD:LED_SK6812_EC15_1.5x1.5mm, F.Cu at (101.9, 130.5)
- added D10: WS6812, LED_SMD:LED_SK6812_EC15_1.5x1.5mm, F.Cu at (101.9, 120.5)
- added D10: WS6812, LED_SMD:LED_SK6812_EC15_1.5x1.5mm, F.Cu at (101.9, 85.5)
- added D10: WS6812, LED_SMD:LED_SK6812_EC15_1.5x1.5mm, F.Cu at (161.9, 60.5)
- added D10: WS6812, LED_SMD:LED_SK6812_EC15_1.5x1.5mm, F.Cu at (161.9, 115.5)
- added D10: WS6812, LED_SMD:LED_SK6812_EC15_1.5x1.5mm, F.Cu at (131.9, 120.5)
- added D10: WS6812, LED_SMD:LED_SK6812_EC15_1.5x1.5mm, F.Cu at (101.9, 60.5)
- added D10: WS6812, LED_SMD:LED_SK6812_EC15_1.5x1.5mm, F.Cu at (131.9, 75.5)
- added D10: WS6812, LED_SMD:LED_SK6812_EC15_1.5x1.5mm, F.Cu at (101.9, 105.5)
- added D10: WS6812, LED_SMD:LED_SK6812_EC15_1.5x1.5mm, F.Cu at (101.9, 95.5)
- added D10: WS6812, LED_SMD:LED_SK6812_EC15_1.5x1.5mm, F.Cu at (131.9, 70.5)
- added D10: WS6812, LED_SMD:LED_SK6812_EC15_1.5x1.5mm, F.Cu at (131.9, 85.5)
- added D10: WS6812, LED_SMD:LED_SK6812_EC15_1.5x1.5mm, F.Cu at (131.9, 125.5)
- added D10: WS6812, LED_SMD:LED_SK6812_EC15_1.5x1.5mm, F.Cu at (131.9, 95.5)
- added D10: WS6812, LED_SMD:LED_SK6812_EC15_1.5x1.5mm, F.Cu at (101.9, 135.5)
- added D10: WS6812, LED_SMD:LED_SK6812_EC15_1.5x1.5mm, F.Cu at (161.9, 125.5)
- added D10: WS6812, LED_SMD:LED_SK6812_EC15_1.5x1.5mm, F.Cu at (131.9, 55.5)
- added D10: WS6812, LED_SMD:LED_SK6812_EC15_1.5x1.5mm, F.Cu at (131.9, 50.5)
- added D10: WS6812, LED_SMD:LED_SK6812_EC15_1.5x1.5mm, F.Cu at (101.9, 80.5)
- added D10: WS6812, LED_SMD:LED_SK6812_EC15_1.5x1.5mm, F.Cu at (131.9, 110.5)
- added D10: WS6812, LED_SMD:LED_SK6812_EC15_1.5x1.5mm, F.Cu at (161.9, 50.5)
- added D10: WS6812, LED_SMD:LED_SK6812_EC15_1.5x1.5mm, F.Cu at (131.9, 135.5)
- added D10: WS6812, LED_SMD:LED_SK6812_EC15_1.5x1.5mm, F.Cu at (101.9, 65.5)
- added D10: WS6812, LED_SMD:LED_SK6812_EC15_1.5x1.5mm, F.Cu at (101.9, 125.5)
- added D10: WS6812, LED_SMD:LED_SK6812_EC15_1.5x1.5mm, F.Cu at (101.9, 55.5)
- added D10: WS6812, LED_SMD:LED_SK6812_EC15_1.5x1.5mm, F.Cu at (161.9, 105.5)
- added D10: WS6812, LED_SMD:LED_SK6812_EC15_1.5x1.5mm, F.Cu at (101.9, 115.5)
- added D10: WS6812, LED_SMD:LED_SK6812_EC15_1.5x1.5mm, F.Cu at (161.9, 70.5)
- added D10: WS6812, LED_SMD:LED_SK6812_EC15_1.5x1.5mm, F.Cu at (101.9, 75.5)
- added D10: WS6812, LED_SMD:LED_SK6812_EC15_1.5x1.5mm, F.Cu at (131.9, 65.5)
- added D11: WS6812, LED_SMD:LED_SK6812_EC15_1.5x1.5mm, F.Cu at (100.1, 115.5)
- added D11: WS6812, LED_SMD:LED_SK6812_EC15_1.5x1.5mm, F.Cu at (160.1, 105.5)
- added D11: WS6812, LED_SMD:LED_SK6812_EC15_1.5x1.5mm, F.Cu at (100.1, 85.5)
- added D11: WS6812, LED_SMD:LED_SK6812_EC15_1.5x1.5mm, F.Cu at (130.1, 125.5)
- added D11: WS6812, LED_SMD:LED_SK6812_EC15_1.5x1.5mm, F.Cu at (130.1, 120.5)
- added D11: WS6812, LED_SMD:LED_SK6812_EC15_1.5x1.5mm, F.Cu at (160.1, 80.5)
- added D11: WS6812, LED_SMD:LED_SK6812_EC15_1.5x1.5mm, F.Cu at (100.1, 95.5)
- added D11: WS6812, LED_SMD:LED_SK6812_EC15_1.5x1.5mm, F.Cu at (130.1, 70.5)
- added D11: WS6812, LED_SMD:LED_SK6812_EC15_1.5x1.5mm, F.Cu at (160.1, 65.5)
- added D11: WS6812, LED_SMD:LED_SK6812_EC15_1.5x1.5mm, F.Cu at (100.1, 60.5)
- added D11: WS6812, LED_SMD:LED_SK6812_EC15_1.5x1.5mm, F.Cu at (130.1, 80.5)
- added D11: WS6812, LED_SMD:LED_SK6812_EC15_1.5x1.5mm, F.Cu at (130.1, 90.5)
- added D11: WS6812, LED_SMD:LED_SK6812_EC15_1.5x1.5mm, F.Cu at (160.1, 90.5)
- added D11: WS6812, LED_SMD:LED_SK6812_EC15_1.5x1.5mm, F.Cu at (130.1, 95.5)
- added D11: WS6812, LED_SMD:LED_SK6812_EC15_1.5x1.5mm, F.Cu at (160.1, 95.5)
- added D11: WS6812, LED_SMD:LED_SK6812_EC15_1.5x1.5mm, F.Cu at (160.1, 115.5)
- added D11: WS6812, LED_SMD:LED_SK6812_EC15_1.5x1.5mm, F.Cu at (160.1, 110.5)
- added D11: WS6812, LED_SMD:LED_SK6812_EC15_1.5x1.5mm, F.Cu at (130.1, 65.5)
- added D11: WS6812, LED_SMD:LED_SK6812_EC15_1.5x1.5mm, F.Cu at (100.1, 120.5)
- added D11: WS6812, LED_SMD:LED_SK6812_EC15_1.5x1.5mm, F.Cu at (130.1, 105.5)
- added D11: WS6812, LED_SMD:LED_SK6812_EC15_1.5x1.5mm, F.Cu at (160.1, 135.5)
- added D11: WS6812, LED_SMD:LED_SK6812_EC15_1.5x1.5mm, F.Cu at (130.1, 135.5)
- added D11: WS6812, LED_SMD:LED_SK6812_EC15_1.5x1.5mm, F.Cu at (100.1, 110.5)
- added D11: WS6812, LED_SMD:LED_SK6812_EC15_1.5x1.5mm, F.Cu at (100.1, 130.5)
- added D11: WS6812, LED_SMD:LED_SK6812_EC15_1.5x1.5mm, F.Cu at (100.1, 75.5)
- added D11: WS6812, LED_SMD:LED_SK6812_EC15_1.5x1.5mm, F.Cu at (160.1, 55.5)
- added D11: WS6812, LED_SMD:LED_SK6812_EC15_1.5x1.5mm, F.Cu at (130.1, 85.5)
- added D11: WS6812, LED_SMD:LED_SK6812_EC15_1.5x1.5mm, F.Cu at (160.1, 70.5)
- added D11: WS6812, LED_SMD:LED_SK6812_EC15_1.5x1.5mm, F.Cu at (160.1, 100.5)
- added D11: WS6812, LED_SMD:LED_SK6812_EC15_1.5x1.5mm, F.Cu at (100.1, 100.5)
- added D11: WS6812, LED_SMD:LED_SK6812_EC15_1.5x1.5mm, F.Cu at (100.1, 70.5)
- added D11: WS6812, LED_SMD:LED_SK6812_EC15_1.5x1.5mm, F.Cu at (130.1, 50.5)
- added D11: WS6812, LED_SMD:LED_SK6812_EC15_1.5x1.5mm, F.Cu at (160.1, 125.5)
- added D11: WS6812, LED_SMD:LED_SK6812_EC15_1.5x1.5mm, F.Cu at (130.1, 75.5)
- added D11: WS6812, LED_SMD:LED_SK6812_EC15_1.5x1.5mm, F.Cu at (100.1, 65.5)
- added D11: WS6812, LED_SMD:LED_SK6812_EC15_1.5x1.5mm, F.Cu at (100.1, 50.5)
- added D11: WS6812, LED_SMD:LED_SK6812_EC15_1.5x1.5mm, F.Cu at (130.1, 110.5)
- added D11: WS6812, LED_SMD:LED_SK6812_EC15_1.5x1.5mm, F.Cu at (100.1, 125.5)
- added D11: WS6812, LED_SMD:LED_SK6812_EC15_1.5x1.5mm, F.Cu at (160.1, 85.5)
- added D11: WS6812, LED_SMD:LED_SK6812_EC15_1.5x1.5mm, F.Cu at (130.1, 60.5)
- added D11: WS6812, LED_SMD:LED_SK6812_EC15_1.5x1.5mm, F.Cu at (100.1, 90.5)
- added D11: WS6812, LED_SMD:LED_SK6812_EC15_1.5x1.5mm, F.Cu at (100.1, 105.5)
- added D11: WS6812, LED_SMD:LED_SK6812_EC15_1.5x1.5mm, F.Cu at (130.1, 130.5)
- added D11: WS6812, LED_SMD:LED_SK6812_EC15_1.5x1.5mm, F.Cu at (100.1, 135.5)
- added D11: WS6812, LED_SMD:LED_SK6812_EC15_1.5x1.5mm, F.Cu at (160.1, 75.5)
- added D11: WS6812, LED_SMD:LED_SK6812_EC15_1.5x1.5mm, F.Cu at (130.1, 100.5)
- added D11: WS6812, LED_SMD:LED_SK6812_EC15_1.5x1.5mm, F.Cu at (100.1, 80.5)
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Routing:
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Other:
- outline, holes or cut-outs redrawn
- board text added: "+"
- board text added: "-"
- board text added: "S"
